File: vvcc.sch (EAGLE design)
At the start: 51 parts, among them IC1 MCP40D19T-5K, IC2 RP2040, IC3 NCP1117LPST33T3G, IC4 16MB_Flash, IC5 LD117ADT-TR, IC6 CLXC8T245QRHLRQ1, J1 Micro-B, J2 302-S301, J3 302-S301, Q1 12MHz

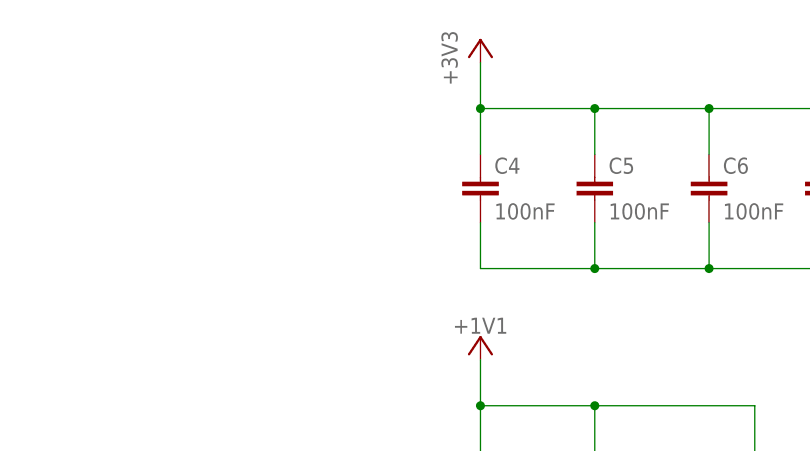
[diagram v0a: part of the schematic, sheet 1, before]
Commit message: Add in a missing 0.1uF capacitor on +3v3
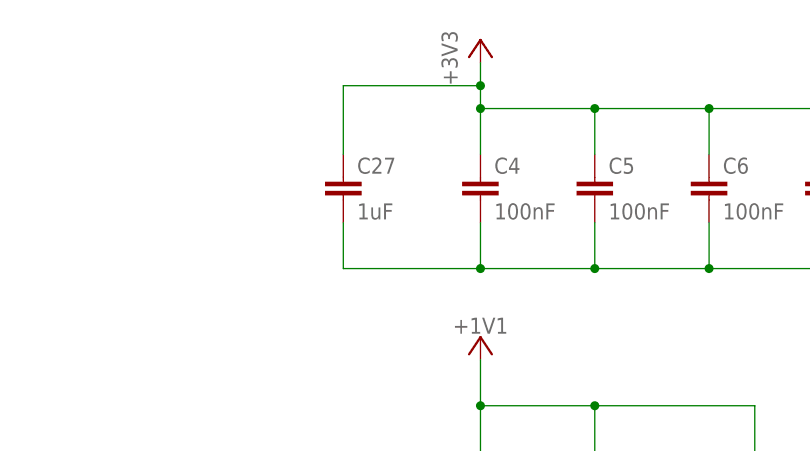
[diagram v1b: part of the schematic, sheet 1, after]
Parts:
- added C27: 1uF, rcl:C-EUC0201
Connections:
- net +3V3: now also C27.1
- net GND: now also C27.2
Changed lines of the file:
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@@
 <setting verticaltext="up"/>
 </settings>
-<grid distance="0.1" unitdist="inch" unit="inch" style="lines" multiple="1" display="yes" altdistance="0.01" altunitdist="inch" altunit="inch"/>
+<grid distance="0.1" unitdist="inch" unit="inch" style="lines" multiple="1" display="no" altdistance="0.01" altunitdist="inch" altunit="inch"/>
 <layers>
 <layer number="1" name="Top" color="4" fill="1" visible="no" active="no"/>
@@
 <part name="+3V9" library="sjg-supply1" deviceset="+3V3" device=""/>
 <part name="SUPPLY15" library="supply2" library_urn="urn:adsk.eagle:library:372" deviceset="GND" device=""/>
+<part name="C27" library="rcl" library_urn="urn:adsk.eagle:library:334" deviceset="C-EU" device="C0201" package3d_urn="urn:adsk.eagle:package:23690/2" value="1uF">
+<spice>
+<pinmapping spiceprefix="C">
+<pinmap gate="G$1" pin="1" pinorder="1"/>
+<pinmap gate="G$1" pin="2" pinorder="2"/>
+</pinmapping>
+</spice>
+<attribute name="USE" value="0201B102K250CT"/>
+</part>
 </parts>
 <sheets>
@@
 <instance part="SUPPLY12" gate="GND" x="170.18" y="43.18" smashed="yes">
 <attribute name="VALUE" x="168.275" y="40.005" size="1.778" layer="96"/>
+</instance>
+<instance part="C27" gate="G$1" x="251.46" y="228.6" smashed="yes" grouprefs="DECOUPLING">
+<attribute name="NAME" x="252.984" y="228.981" size="1.778" layer="95"/>
+<attribute name="VALUE" x="252.984" y="223.901" size="1.778" layer="96"/>
+<attribute name="USE" x="251.46" y="228.6" size="1.778" layer="96" display="off"/>
 </instance>
 </instances>
@@
 <junction x="342.9" y="218.44" grouprefs="DECOUPLING"/>
 <junction x="355.6" y="218.44" grouprefs="DECOUPLING"/>
+<pinref part="C27" gate="G$1" pin="2"/>
+<wire x1="251.46" y1="223.52" x2="251.46" y2="218.44" width="0.1524" layer="91"/>
+<wire x1="251.46" y1="218.44" x2="266.7" y2="218.44" width="0.1524" layer="91"/>
+<junction x="266.7" y="218.44"/>
 </segment>
 <segment>
@@
 <junction x="330.2" y="236.22" grouprefs="DECOUPLING"/>
 <pinref part="+3V3" gate="G$1" pin="+3V3"/>
-<wire x1="266.7" y1="236.22" x2="266.7" y2="241.3" width="0.1524" layer="91" grouprefs="DECOUPLING"/>
+<wire x1="266.7" y1="236.22" x2="266.7" y2="238.76" width="0.1524" layer="91" grouprefs="DECOUPLING"/>
 <pinref part="C14" gate="G$1" pin="1"/>
+<wire x1="266.7" y1="238.76" x2="266.7" y2="241.3" width="0.1524" layer="91" grouprefs="DECOUPLING"/>
 <wire x1="342.9" y1="236.22" x2="355.6" y2="236.22" width="0.1524" layer="91" grouprefs="DECOUPLING"/>
 <wire x1="355.6" y1="236.22" x2="355.6" y2="231.14" width="0.1524" layer="91" grouprefs="DECOUPLING"/>
@@
 <wire x1="368.3" y1="236.22" x2="368.3" y2="231.14" width="0.1524" layer="91" grouprefs="DECOUPLING"/>
 <junction x="355.6" y="236.22" grouprefs="DECOUPLING"/>
-</segment>
-<segment>
+<pinref part="C27" gate="G$1" pin="1"/>
+<wire x1="266.7" y1="238.76" x2="251.46" y2="238.76" width="0.1524" layer="91"/>
+<wire x1="251.46" y1="238.76" x2="251.46" y2="231.14" width="0.1524" layer="91"/>
+<junction x="266.7" y="238.76"/>
+</segment>
+<segment>

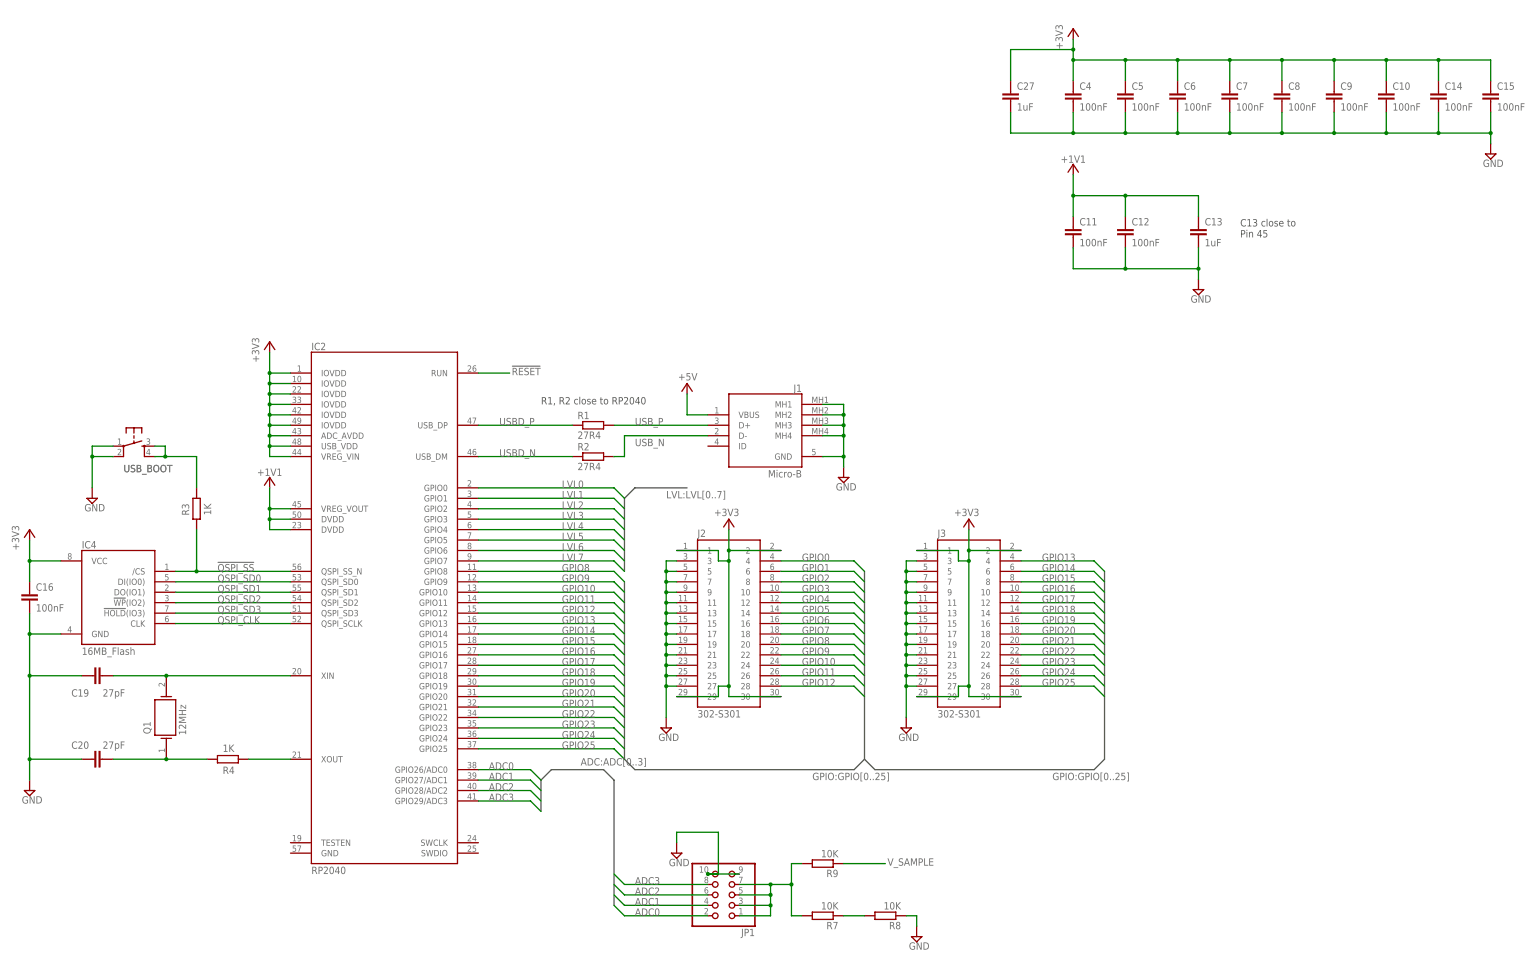
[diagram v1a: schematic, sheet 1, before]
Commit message: Fix a few errors in the schematic. It is good to connect GND to the chip...
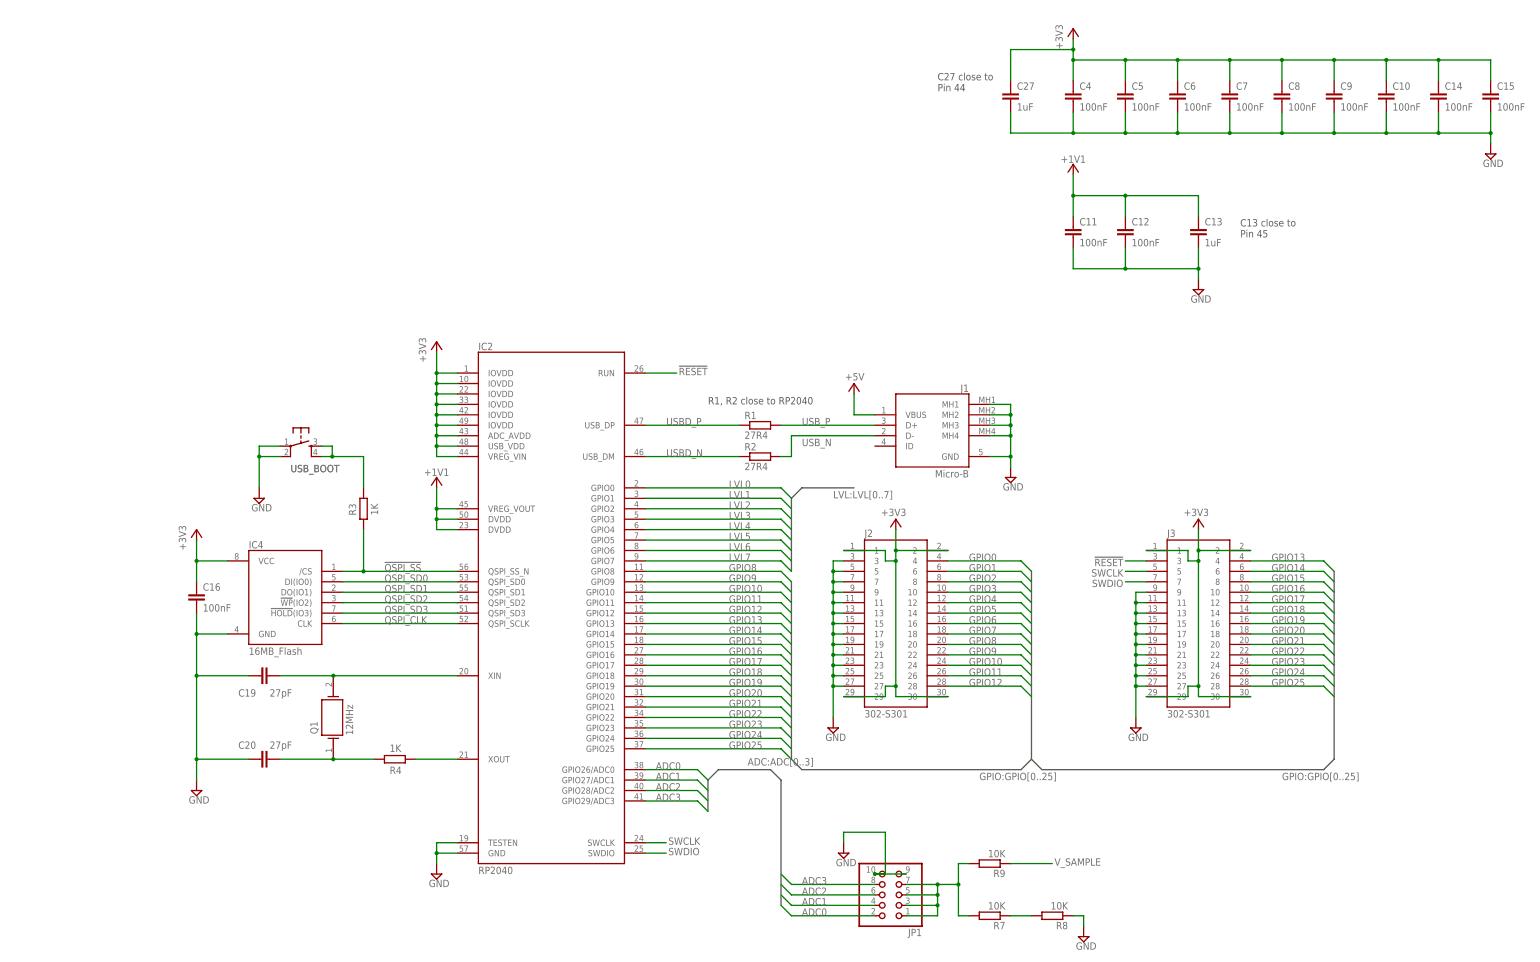
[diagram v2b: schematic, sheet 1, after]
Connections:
- new net SWCLK: IC2.SWCLK, J3.5
- new net SWDIO: IC2.SWDIO, J3.7
- net !RESET!: now also J3.3
- net GND: now also IC2.GND, IC2.TESTEN; no longer J3.3, J3.5, J3.7
- net GPIO8: now also IC6.DIR
- net GPIO9: now also IC6.!OE
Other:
- note added: "C27 close to Pin 44"
- moved on the sheet: C16, C19, C20, IC2, IC4, J1, J2, J3, JP1, Q1, R1, R2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

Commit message: Make sure everything has a USE attribute
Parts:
- IC2: USE (none) -> SC0914(13)
- IC6: USE (none) -> CLXC8T245QRHLRQ1
- J2, J3: USE (none) -> 302-S301
- JP1: USE (none) -> TSHS-105-D-06-A-T-LF
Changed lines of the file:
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@@
 <setting verticaltext="up"/>
 </settings>
-<grid distance="0.1" unitdist="inch" unit="inch" style="lines" multiple="1" display="yes" altdistance="0.01" altunitdist="inch" altunit="inch"/>
+<grid distance="0.1" unitdist="inch" unit="inch" style="lines" multiple="1" display="no" altdistance="0.01" altunitdist="inch" altunit="inch"/>
 <layers>
 <layer number="1" name="Top" color="4" fill="1" visible="no" active="no"/>
@@
 <part name="SUPPLY1" library="supply2" library_urn="urn:adsk.eagle:library:372" deviceset="GND" device=""/>
 <part name="P+2" library="sjg-supply1" deviceset="+5V" device=""/>
-<part name="IC2" library="samacsys" deviceset="RP2040" device=""/>
+<part name="IC2" library="samacsys" deviceset="RP2040" device="">
+<attribute name="USE" value="SC0914(13)"/>
+</part>
 <part name="+3V1" library="sjg-supply1" deviceset="+3V3" device=""/>
 <part name="U$1" library="sjg-supply1" deviceset="+1V1" device=""/>
@@
 <attribute name="USE" value="C0201C270J3GAC7867"/>
 </part>
-<part name="J2" library="samacsys" deviceset="302-S301" device=""/>
-<part name="J3" library="samacsys" deviceset="302-S301" device=""/>
+<part name="J2" library="samacsys" deviceset="302-S301" device="">
+<attribute name="USE" value="302-S301"/>
+</part>
+<part name="J3" library="samacsys" deviceset="302-S301" device="">
+<attribute name="USE" value="302-S301"/>
+</part>
 <part name="SUPPLY9" library="supply2" library_urn="urn:adsk.eagle:library:372" deviceset="GND" device=""/>
 <part name="+3V5" library="supply1" library_urn="urn:adsk.eagle:library:371" deviceset="+3V3" device=""/>
@@
 </part>
 <part name="SUPPLY11" library="supply2" library_urn="urn:adsk.eagle:library:372" deviceset="GND" device=""/>
-<part name="JP1" library="pinhead" library_urn="urn:adsk.eagle:library:325" deviceset="PINHD-2X5" device="" package3d_urn="urn:adsk.eagle:package:22470/2"/>
+<part name="JP1" library="pinhead" library_urn="urn:adsk.eagle:library:325" deviceset="PINHD-2X5" device="" package3d_urn="urn:adsk.eagle:package:22470/2">
+<attribute name="USE" value="TSHS-105-D-06-A-T-LF"/>
+</part>
 <part name="SUPPLY12" library="supply2" library_urn="urn:adsk.eagle:library:372" deviceset="GND" device=""/>
 <part name="IC5" library="v-reg" library_urn="urn:adsk.eagle:library:409" deviceset="LD117A?*" device="DT" package3d_urn="urn:adsk.eagle:package:30369/1" technology="-TR">
@@
 </part>
 <part name="FRAME2" library="frames" library_urn="urn:adsk.eagle:library:229" deviceset="A3L-LOC" device=""/>
-<part name="IC6" library="samacsys" deviceset="CLXC8T245QRHLRQ1" device=""/>
+<part name="IC6" library="samacsys" deviceset="CLXC8T245QRHLRQ1" device="">
+<attribute name="USE" value="CLXC8T245QRHLRQ1"/>
+</part>
 <part name="+3V8" library="sjg-supply1" deviceset="+3V3" device=""/>
 <part name="SUPPLY13" library="supply2" library_urn="urn:adsk.eagle:library:372" deviceset="GND" device=""/>
@@
 <attribute name="NAME" x="121.92" y="165.608" size="1.778" layer="95"/>
 <attribute name="VALUE" x="121.92" y="38.1" size="1.778" layer="96"/>
+<attribute name="USE" x="139.7" y="104.14" size="1.778" layer="96" display="off"/>
 </instance>
 <instance part="+3V1" gate="G$1" x="111.76" y="167.64" smashed="yes">
@@
 <attribute name="NAME" x="215.9" y="120.142" size="1.778" layer="95"/>
 <attribute name="VALUE" x="215.9" y="76.2" size="1.778" layer="96"/>
+<attribute name="USE" x="223.52" y="99.06" size="1.778" layer="96" display="off"/>
 </instance>
 <instance part="J3" gate="G$1" x="297.18" y="99.06" smashed="yes">
 <attribute name="NAME" x="289.56" y="120.142" size="1.778" layer="95"/>
 <attribute name="VALUE" x="289.56" y="76.2" size="1.778" layer="96"/>
+<attribute name="USE" x="297.18" y="99.06" size="1.778" layer="96" display="off"/>
 </instance>
 <instance part="SUPPLY9" gate="GND" x="208.28" y="73.66" smashed="yes">
@@
 <attribute name="NAME" x="229.87" y="24.765" size="1.778" layer="95" rot="R180"/>
 <attribute name="VALUE" x="229.87" y="43.18" size="1.778" layer="96" rot="R180"/>
+<attribute name="USE" x="223.52" y="33.02" size="1.778" layer="96" rot="R180" display="off"/>
 </instance>
 <instance part="SUPPLY12" gate="GND" x="210.82" y="43.18" smashed="yes">
@@
 <attribute name="NAME" x="63.5" y="152.908" size="1.778" layer="95"/>
 <attribute name="VALUE" x="63.5" y="91.44" size="1.778" layer="96"/>
+<attribute name="USE" x="73.66" y="124.46" size="1.778" layer="96" display="off"/>
 </instance>
 <instance part="IC1" gate="G$1" x="223.52" y="226.06" smashed="yes">

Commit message: Submit for creation
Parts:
- C17: device rcl:C-EUC0402K -> rcl:C-EUC0402; USE CL05A106MP5NUNC -> GRM155R60J106ME15D
- C18: USE GRM033R61A104ME15D -> 0201X104M160CT
- JP1: value (none) -> ADC_IO; USE TSHS-105-D-06-A-T-LF -> PR20205VBDN
- RESET: value RESET -> B3F-1005
- USB_BOOT: value USB_BOOT -> B3F-1005
